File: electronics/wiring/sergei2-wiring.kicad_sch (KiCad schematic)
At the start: 36 parts, among them J1 6i25 port 1, J2 6i25 port 2, M1 UGRMEM, M101 Enclosure Fan, M102 Coolant Pump, M2 UGRMEM, M3 57BLF02, M4 Spindle, SW1 ESTOP, SW2 Mode switch, SW3 Run, SW4 Door closed, SW5 Pause, SW7 50°C NO, U1 Power_control_PCB, U3 BrakeShunt

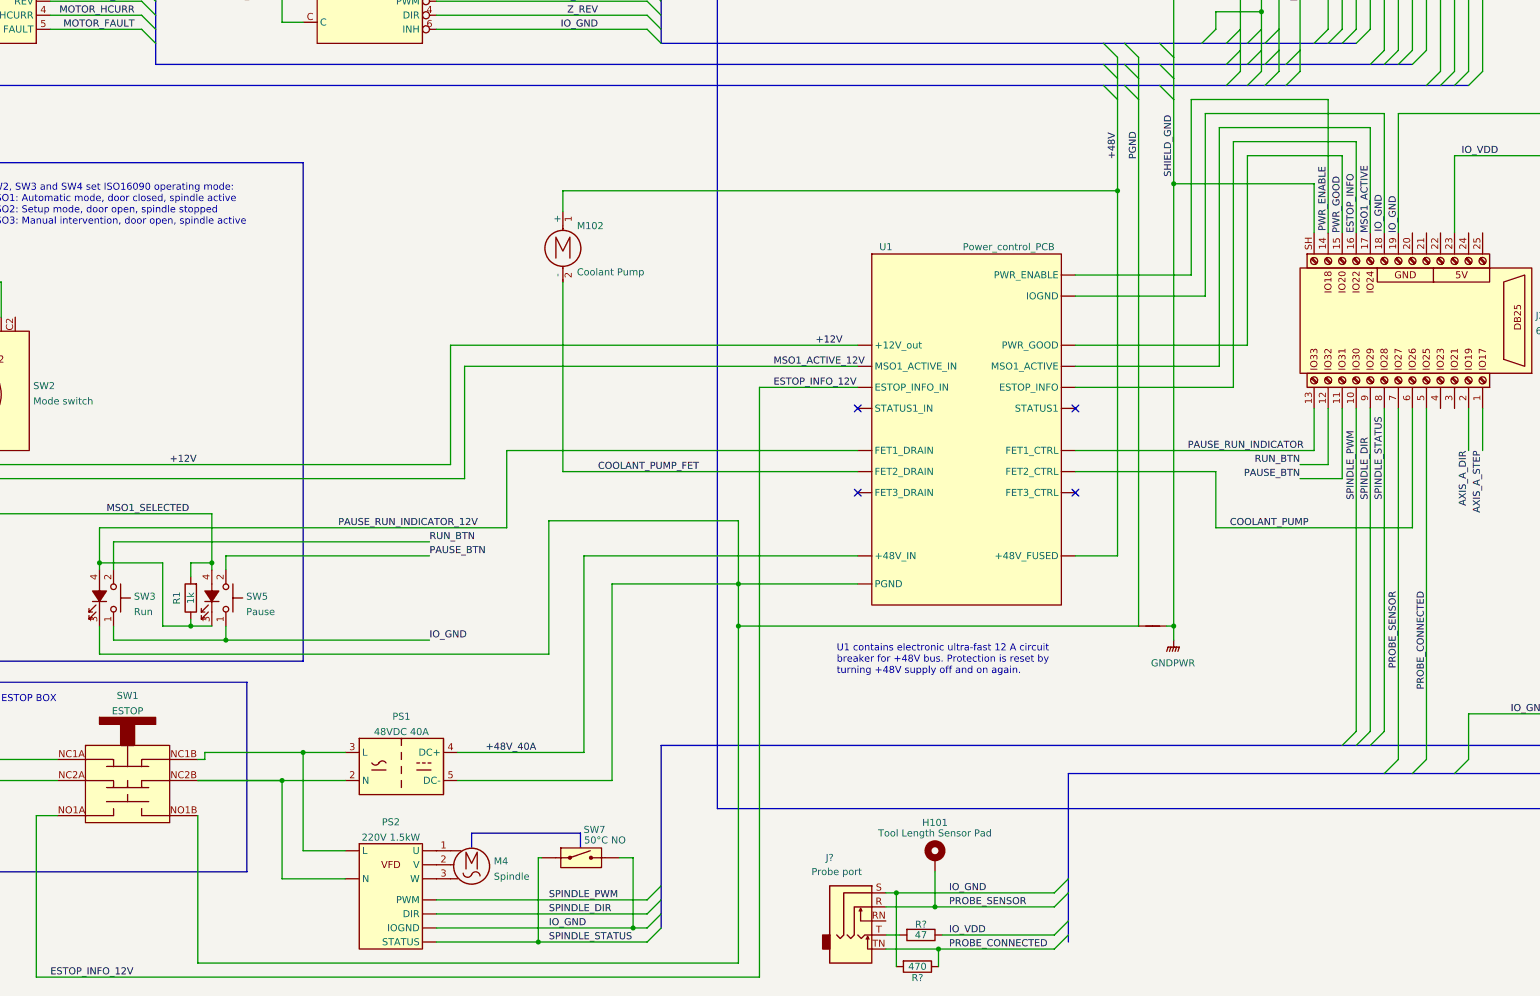
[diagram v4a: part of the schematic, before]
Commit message: Dont start spindle when probe connected
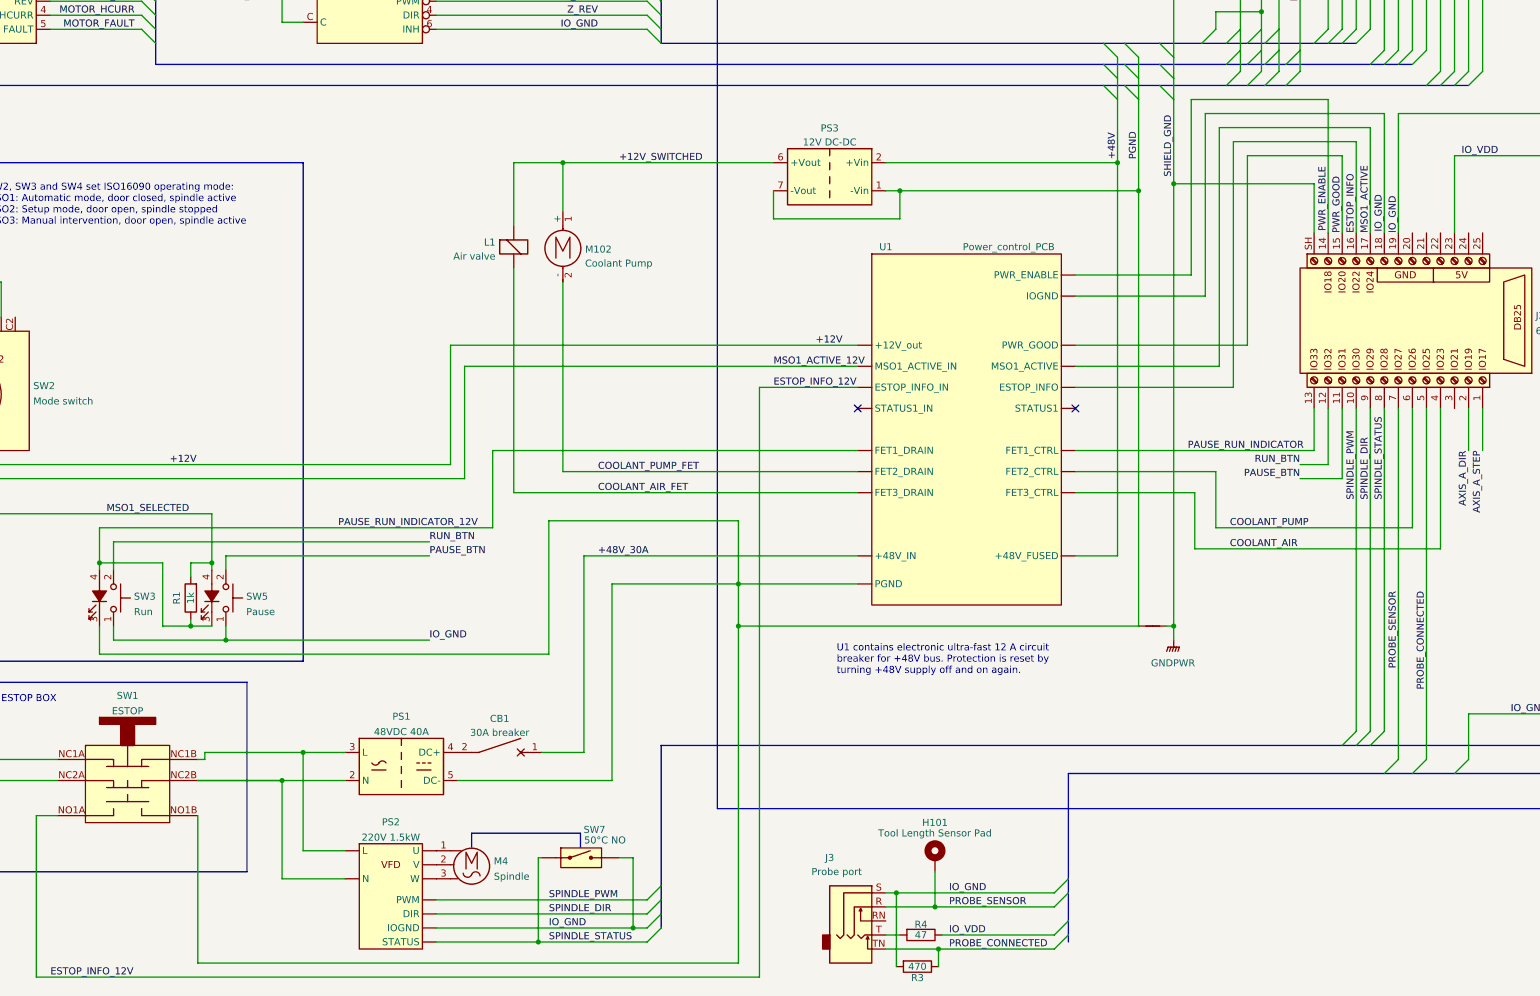
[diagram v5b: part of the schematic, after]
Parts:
- added CB1: 30A breaker, symbol Device:CircuitBreaker_1P
- added L1: Air valve, symbol Device:ElectromagneticActor
- added PS3: 12V DC-DC, Converter_DCDC:Converter_DCDC_XP_POWER-ITXxxxxSA_THT, symbol Converter_DCDC:ITX4812SA
- gave numbers to parts that had none: 3
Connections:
- net +48V: now also PS3.2 (+Vin); no longer M102.1 (+)
- net PGND: now also PS3.1 (-Vin), PS3.7 (-Vout)
- net COOLANT_AIR: now reaches J2.4
- net COOLANT_AIR: now also U1. (STATUS1_IN)
- net +48V_40A: no longer names the net of PS1.4 (DC+)
- net +48V_40A: now also CB1.2; no longer U1. (STATUS1_IN)
- new net +12V_SWITCHED: L1.1 (-), M102.1 (+), PS3.6 (+Vout)
- new net +48V_30A: CB1.1, U1. (STATUS1_IN)
- new net COOLANT_AIR_FET: L1.2 (+), U1. (STATUS1_IN)
- no-connect marks 4 -> 2

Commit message: Update wiring diagram
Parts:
- removed M102: Coolant Pump, symbol Motor:Motor_DC
- added M5: Coolant pump, symbol Motor:Stepper_Motor_bipolar
- added U2: Stepper driver, symbol sergei2_wiring:Stepper_driver
- added U4: Pulse counter, symbol sergei2_wiring:Pulse_counter
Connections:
- net COOLANT_PUMP_FET is gone; now on net PWR_GOOD: U1. (STATUS1_IN)
- net +12V_SWITCHED: now also U2. (~{B}), U4. (V-)
- net COOLANT_PUMP: now also J2.3, U2. (~{B}); no longer J2.6, U1. (STATUS1_IN)
- net PGND: now also U2. (~{B})
- new net: M5.1, U2. (~{B})
- new net: M5.2 (-), U2. (~{B})
- new net: M5.3, U2. (~{B})
- new net: M5.4, U2. (~{B})
- new net MINUTE_CNT: J2.6, U1. (STATUS1_IN)
- new net MINUTE_CNT_FET: U1. (STATUS1_IN), U4. (V-)
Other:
- moved on the sheet: M101

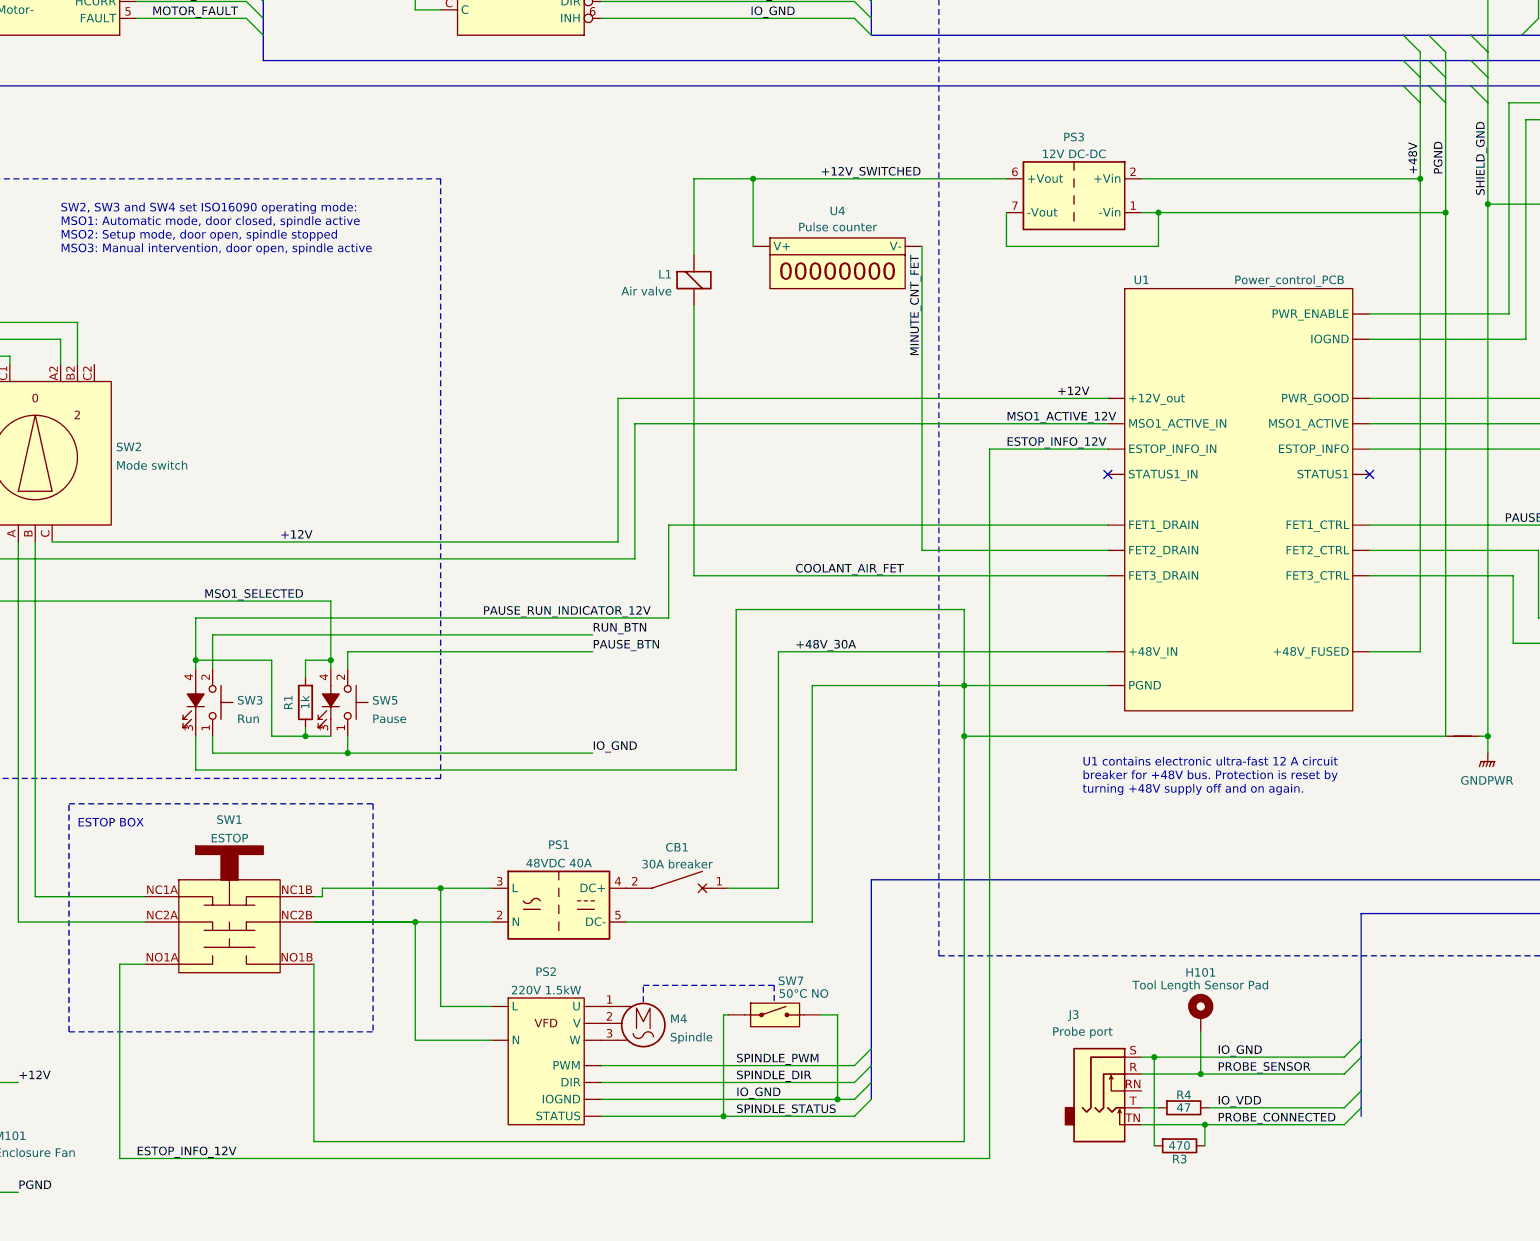
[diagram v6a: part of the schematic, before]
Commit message: Add spindle speed sensor & extra fan (#11, #20)
This should allow monitoring the spindle load level and
to cool it better at low RPM.
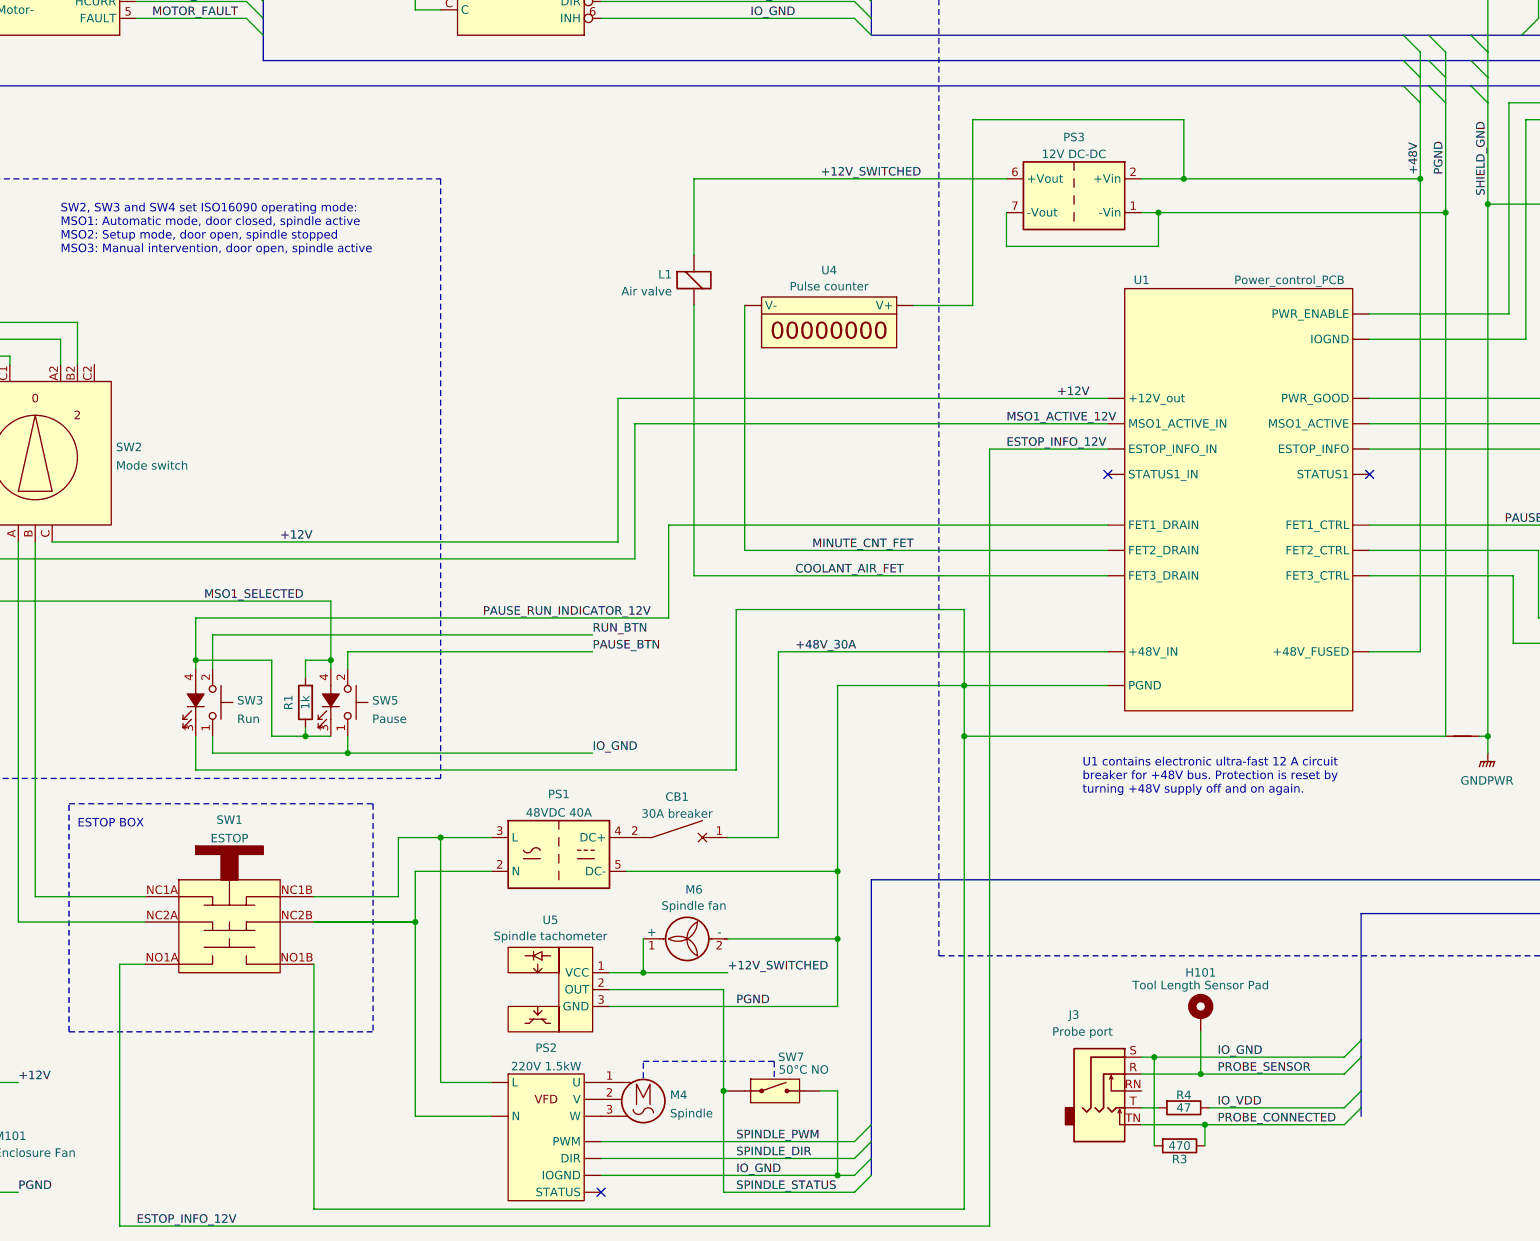
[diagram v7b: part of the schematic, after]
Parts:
- added M6: Spindle fan, symbol Motor:Fan
- added U5: Spindle tachometer, symbol sergei2_wiring:Fork sensor
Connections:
- net +12V_SWITCHED: now also M6.1 (+), U5.1 (VCC); no longer U4. (V-)
- net +48V: now also U4. (V-)
- net PGND: now also M6.2 (-), U5.3 (GND)
- net SPINDLE_STATUS: now also U5.2 (OUT); no longer PS2. (STATUS)
- no-connect marks 2 -> 3
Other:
- moved on the sheet: CB1, M4, PS1, PS2, SW7, U4
